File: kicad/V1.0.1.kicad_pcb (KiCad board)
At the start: 2 copper layers, 49.5 x 38.1 mm, 20 parts, among them IC1 OPA2134P, U1 TLE2426CP

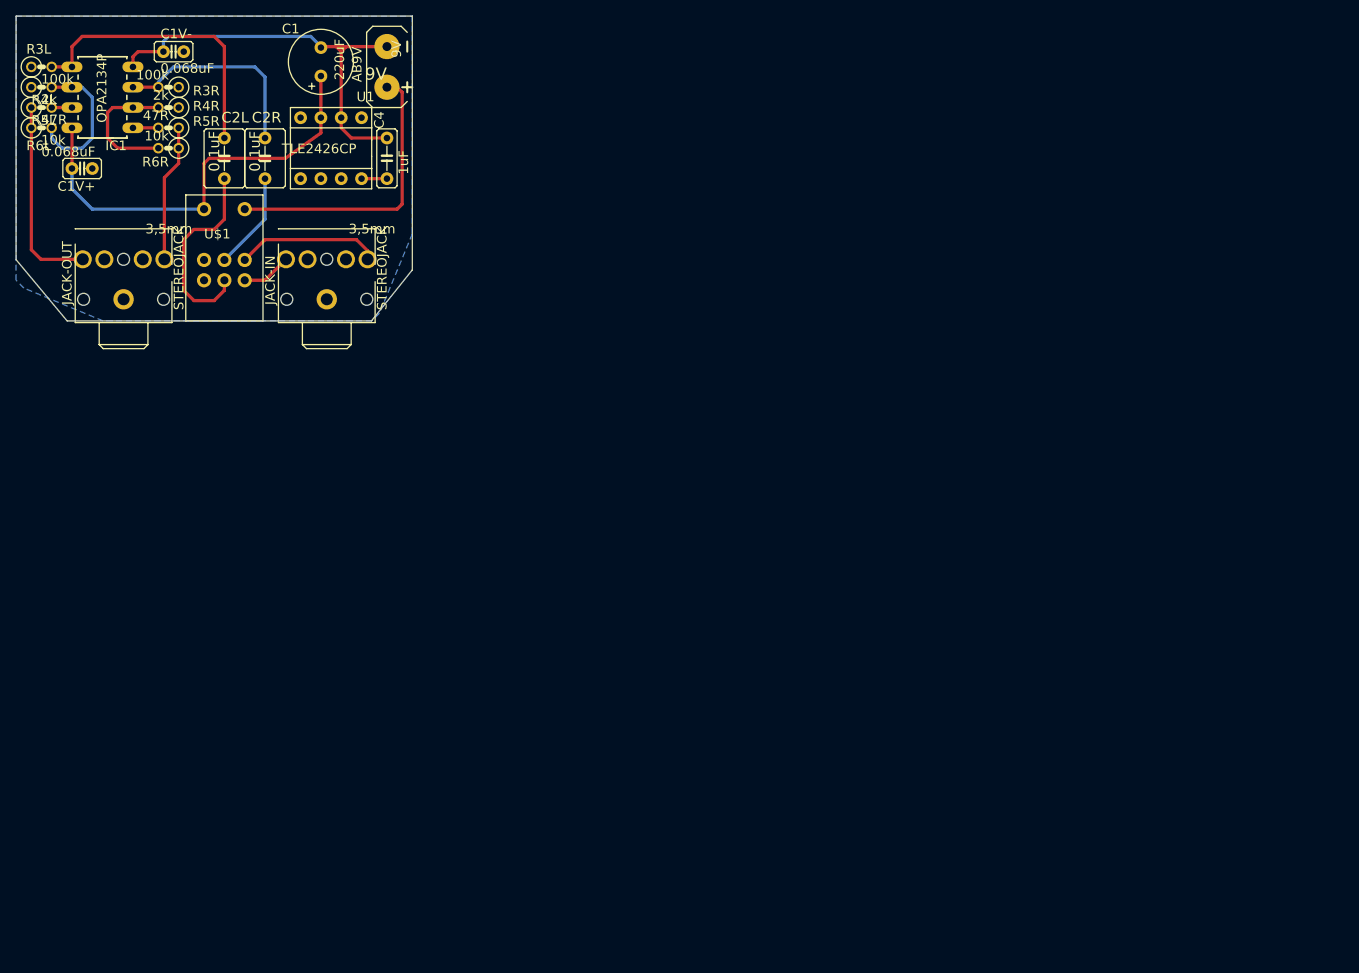
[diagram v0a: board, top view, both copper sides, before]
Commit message: Modified slightly to fix some ERC issues
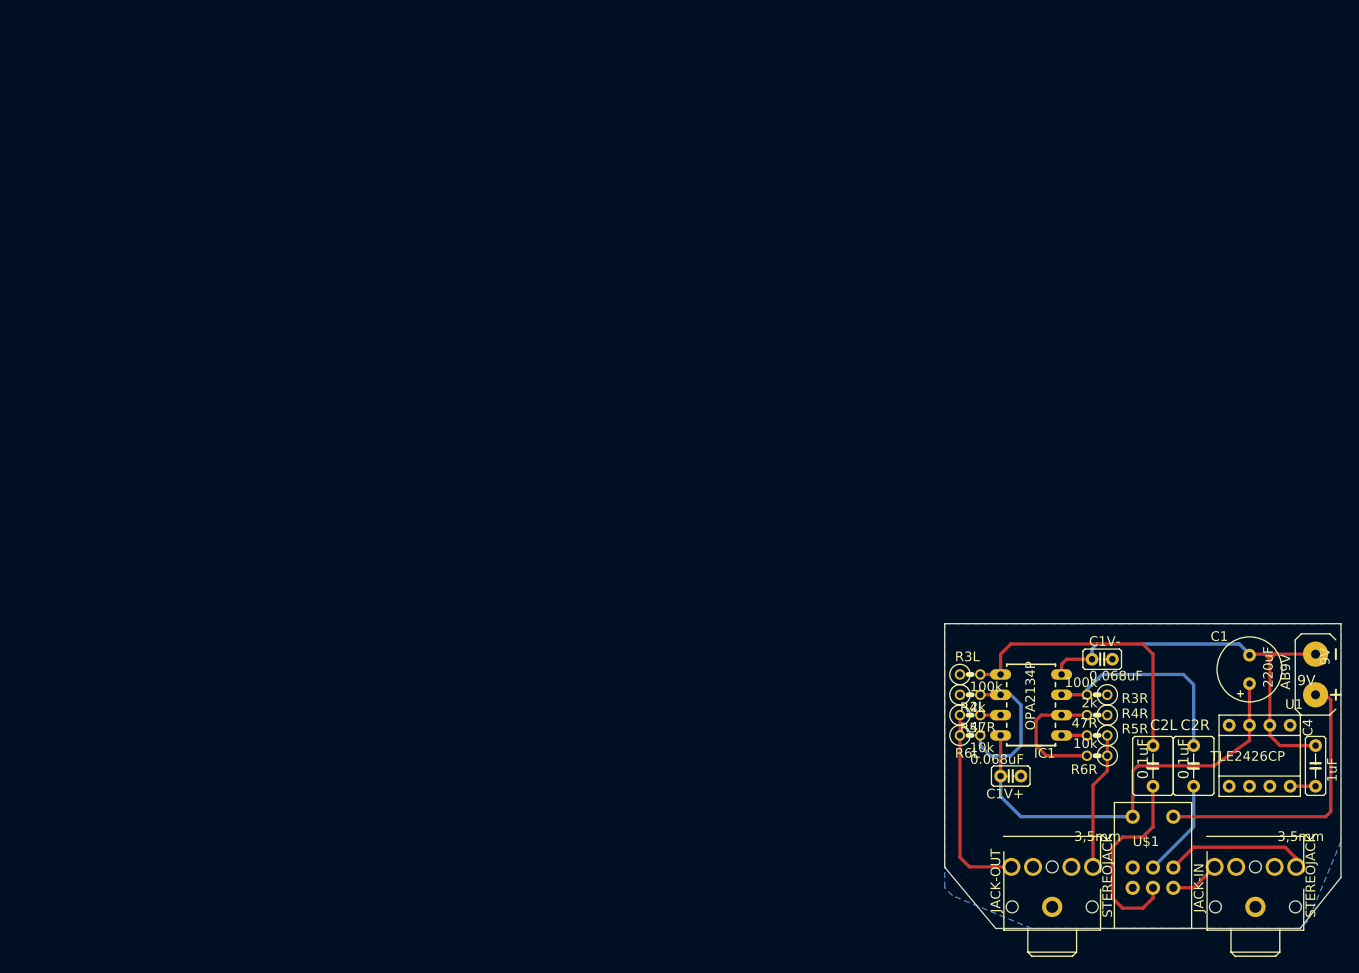
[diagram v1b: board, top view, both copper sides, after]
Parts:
- R3L, R3R, R4L, R4R, R5L, R5R, R6L, R6R: footprint 0207/2V -> 0207_2V
- moved C2R 138.7 mm to (147.2, 55.6)
- moved 9V 138.7 mm to (162.4, 44.2)
- moved C1 138.7 mm to (154.2, 43.6)
- moved C1V+ 138.7 mm to (124.3, 56.9)
- moved C1V- 138.7 mm to (135.8, 42.3)
- moved C2L 138.7 mm to (142.1, 55.6)
- moved C4 138.7 mm to (162.4, 55.6)
- moved IC1 138.7 mm to (126.9, 48.0)
- moved JACK-IN 138.7 mm to (154.8, 75.9)
- moved JACK-OUT 138.7 mm to (129.4, 75.9)
- moved R3L 138.7 mm to (119.3, 44.2)
- moved R3R 138.7 mm to (135.1, 46.7)
- moved R4L 138.7 mm to (119.3, 46.7)
- moved R4R 138.7 mm to (135.1, 49.3)
- moved R5L 138.7 mm to (119.3, 49.3)
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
